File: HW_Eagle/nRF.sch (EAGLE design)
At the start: 24 parts, among them X1 B4B-ZR

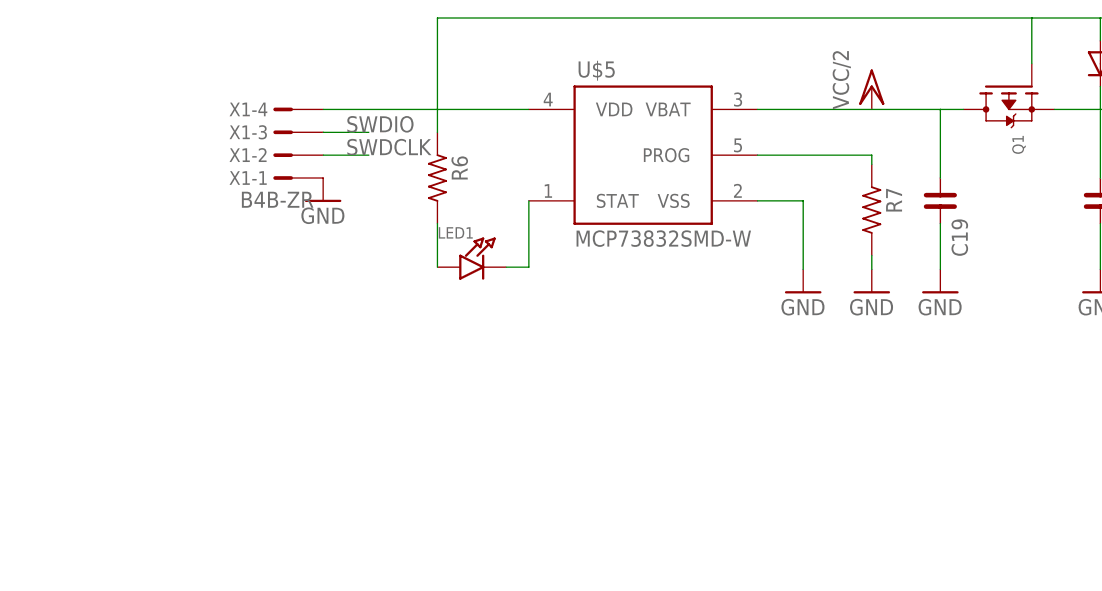
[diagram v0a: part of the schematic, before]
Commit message: [HW] Add Batterry connector
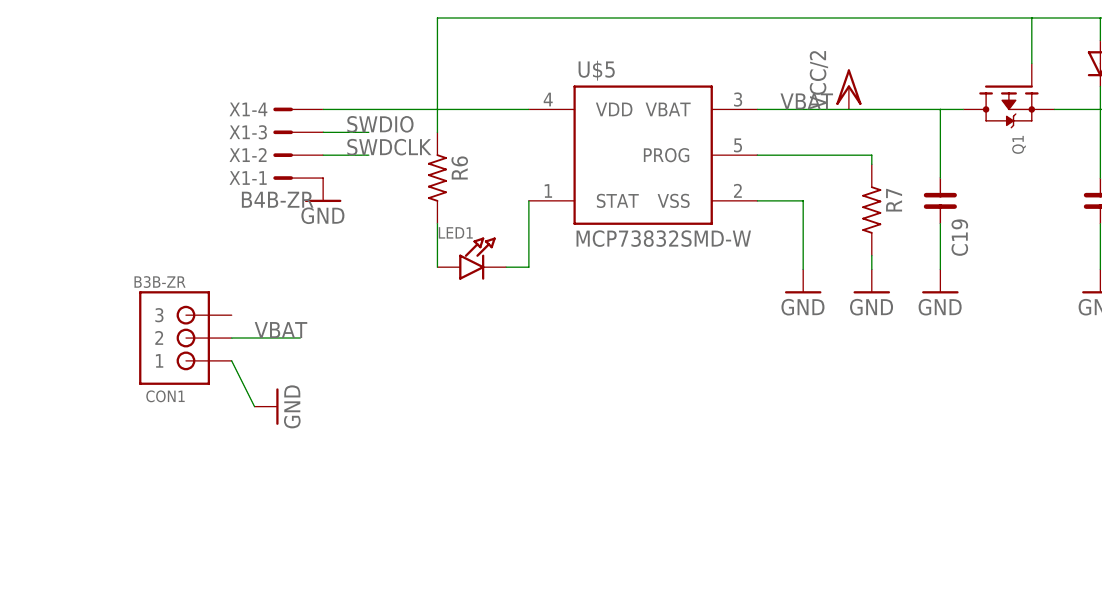
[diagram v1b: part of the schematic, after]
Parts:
- added CON1: B3B-ZR, jst:B3B-ZR
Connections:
- net GND: now also CON1.1
- net VBAT: now also CON1.2
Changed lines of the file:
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@@
 <grid distance="0.1" unitdist="inch" unit="inch" style="lines" multiple="1" display="no" altdistance="0.01" altunitdist="inch" altunit="inch"/>
 <layers>
-<layer number="1" name="Top" color="4" fill="1" visible="yes" active="no"/>
-<layer number="16" name="Bottom" color="1" fill="1" visible="yes" active="no"/>
-<layer number="17" name="Pads" color="2" fill="1" visible="yes" active="no"/>
-<layer number="18" name="Vias" color="2" fill="1" visible="yes" active="no"/>
-<layer number="19" name="Unrouted" color="6" fill="1" visible="yes" active="no"/>
-<layer number="20" name="Dimension" color="15" fill="1" visible="yes" active="no"/>
-<layer number="21" name="tPlace" color="7" fill="1" visible="yes" active="no"/>
-<layer number="22" name="bPlace" color="7" fill="1" visible="yes" active="no"/>
-<layer number="23" name="tOrigins" color="15" fill="1" visible="yes" active="no"/>
-<layer number="24" name="bOrigins" color="15" fill="1" visible="yes" active="no"/>
-<layer number="25" name="tNames" color="7" fill="1" visible="yes" active="no"/>
-<layer number="26" name="bNames" color="7" fill="1" visible="yes" active="no"/>
-<layer number="27" name="tValues" color="7" fill="1" visible="yes" active="no"/>
-<layer number="28" name="bValues" color="7" fill="1" visible="yes" active="no"/>
+<layer number="1" name="Top" color="4" fill="1" visible="no" active="no"/>
+<layer number="16" name="Bottom" color="1" fill="1" visible="no" active="no"/>
+<layer number="17" name="Pads" color="2" fill="1" visible="no" active="no"/>
+<layer number="18" name="Vias" color="2" fill="1" visible="no" active="no"/>
+<layer number="19" name="Unrouted" color="6" fill="1" visible="no" active="no"/>
+<layer number="20" name="Dimension" color="15" fill="1" visible="no" active="no"/>
+<layer number="21" name="tPlace" color="7" fill="1" visible="no" active="no"/>
+<layer number="22" name="bPlace" color="7" fill="1" visible="no" active="no"/>
+<layer number="23" name="tOrigins" color="15" fill="1" visible="no" active="no"/>
+<layer number="24" name="bOrigins" color="15" fill="1" visible="no" active="no"/>
+<layer number="25" name="tNames" color="7" fill="1" visible="no" active="no"/>
+<layer number="26" name="bNames" color="7" fill="1" visible="no" active="no"/>
+<layer number="27" name="tValues" color="7" fill="1" visible="no" active="no"/>
+<layer number="28" name="bValues" color="7" fill="1" visible="no" active="no"/>
 <layer number="29" name="tStop" color="7" fill="3" visible="no" active="no"/>
 <layer number="30" name="bStop" color="7" fill="6" visible="no" active="no"/>
@@
 <layer number="35" name="tGlue" color="7" fill="4" visible="no" active="no"/>
 <layer number="36" name="bGlue" color="7" fill="5" visible="no" active="no"/>
-<layer number="37" name="tTest" color="7" fill="1" visible="yes" active="no"/>
-<layer number="38" name="bTest" color="7" fill="1" visible="yes" active="no"/>
+<layer number="37" name="tTest" color="7" fill="1" visible="no" active="no"/>
+<layer number="38" name="bTest" color="7" fill="1" visible="no" active="no"/>
 <layer number="39" name="tKeepout" color="4" fill="11" visible="no" active="no"/>
 <layer number="40" name="bKeepout" color="1" fill="11" visible="no" active="no"/>
@@
 <layer number="44" name="Drills" color="7" fill="1" visible="no" active="no"/>
 <layer number="45" name="Holes" color="7" fill="1" visible="no" active="no"/>
-<layer number="46" name="Milling" color="3" fill="1" visible="yes" active="no"/>
-<layer number="47" name="Measures" color="7" fill="1" visible="yes" active="no"/>
-<layer number="48" name="Document" color="7" fill="1" visible="yes" active="no"/>
-<layer number="49" name="Reference" color="7" fill="1" visible="yes" active="no"/>
-<layer number="50" name="dxf" color="7" fill="1" visible="yes" active="no"/>
-<layer number="51" name="tDocu" color="7" fill="1" visible="yes" active="no"/>
-<layer number="52" name="bDocu" color="7" fill="1" visible="yes" active="no"/>
-<layer number="53" name="tGND_GNDA" color="7" fill="9" visible="yes" active="no"/>
-<layer number="54" name="bGND_GNDA" color="1" fill="9" visible="yes" active="no"/>
-<layer number="56" name="wert" color="7" fill="1" visible="yes" active="no"/>
+<layer number="46" name="Milling" color="3" fill="1" visible="no" active="no"/>
+<layer number="47" name="Measures" color="7" fill="1" visible="no" active="no"/>
+<layer number="48" name="Document" color="7" fill="1" visible="no" active="no"/>
+<layer number="49" name="Reference" color="7" fill="1" visible="no" active="no"/>
+<layer number="50" name="dxf" color="7" fill="1" visible="no" active="no"/>
+<layer number="51" name="tDocu" color="7" fill="1" visible="no" active="no"/>
+<layer number="52" name="bDocu" color="7" fill="1" visible="no" active="no"/>
+<layer number="53" name="tGND_GNDA" color="7" fill="9" visible="no" active="no"/>
+<layer number="54" name="bGND_GNDA" color="1" fill="9" visible="no" active="no"/>
+<layer number="56" name="wert" color="7" fill="1" visible="no" active="no"/>
 <layer number="90" name="Modules" color="5" fill="1" visible="yes" active="yes"/>
 <layer number="91" name="Nets" color="2" fill="1" visible="yes" active="yes"/>
@@
 <part name="GND1" library="supply1" deviceset="GND" device=""/>
 <part name="GND2" library="supply1" deviceset="GND" device=""/>
+<part name="GND3" library="supply1" deviceset="GND" device=""/>
+<part name="CON1" library="jst" deviceset="B3B-ZR" device=""/>
 </parts>
 <sheets>
@@
 <instance part="GND25" gate="1" x="-83.82" y="165.1"/>
 <instance part="GND26" gate="1" x="-30.48" y="154.94"/>
-<instance part="P+9" gate="G$1" x="-22.86" y="177.8"/>
+<instance part="P+9" gate="G$1" x="-25.4" y="177.8"/>
 <instance part="R6" gate="G$1" x="-71.12" y="167.64" rot="R270"/>
 <instance part="C19" gate="G$1" x="-15.24" y="165.1" rot="R270"/>
@@
 <instance part="GND1" gate="1" x="-17.78" y="93.98" rot="R270"/>
 <instance part="GND2" gate="1" x="-17.78" y="68.58" rot="R270"/>
+<instance part="GND3" gate="1" x="-88.9" y="142.24" rot="R90"/>
+<instance part="CON1" gate="G$1" x="-101.6" y="149.86" rot="R180"/>
 </instances>
 <busses>
@@
 <pinref part="GND2" gate="1" pin="GND"/>
 </segment>
+<segment>
+<pinref part="CON1" gate="G$1" pin="1"/>
+<pinref part="GND3" gate="1" pin="GND"/>
+<wire x1="-91.44" y1="142.24" x2="-93.98" y2="147.32" width="0.1524" layer="91"/>
+</segment>
 </net>
 <net name="VCC" class="0">
@@
 <segment>
 <pinref part="U$5" gate="G$1" pin="VBAT"/>
-<wire x1="-22.86" y1="175.26" x2="-35.56" y2="175.26" width="0.1524" layer="91"/>
+<wire x1="-25.4" y1="175.26" x2="-35.56" y2="175.26" width="0.1524" layer="91"/>
 <pinref part="P+9" gate="G$1" pin="VCC/2"/>
 <pinref part="C19" gate="G$1" pin="1"/>
-<wire x1="-22.86" y1="175.26" x2="-15.24" y2="175.26" width="0.1524" layer="91"/>
+<wire x1="-25.4" y1="175.26" x2="-15.24" y2="175.26" width="0.1524" layer="91"/>
 <wire x1="-15.24" y1="175.26" x2="-15.24" y2="167.64" width="0.1524" layer="91"/>
 <pinref part="Q1" gate="G$1" pin="D"/>
 <wire x1="-12.7" y1="175.26" x2="-15.24" y2="175.26" width="0.1524" layer="91"/>
-</segment>
-</net>
+<label x="-33.02" y="175.26" size="1.778" layer="95"/>
+</segment>
+<segment>
+<pinref part="CON1" gate="G$1" pin="2"/>
+<wire x1="-86.36" y1="149.86" x2="-93.98" y2="149.86" width="0.1524" layer="91"/>
+<label x="-91.44" y="149.86" size="1.778" layer="95"/>
+</segment>
+</net>

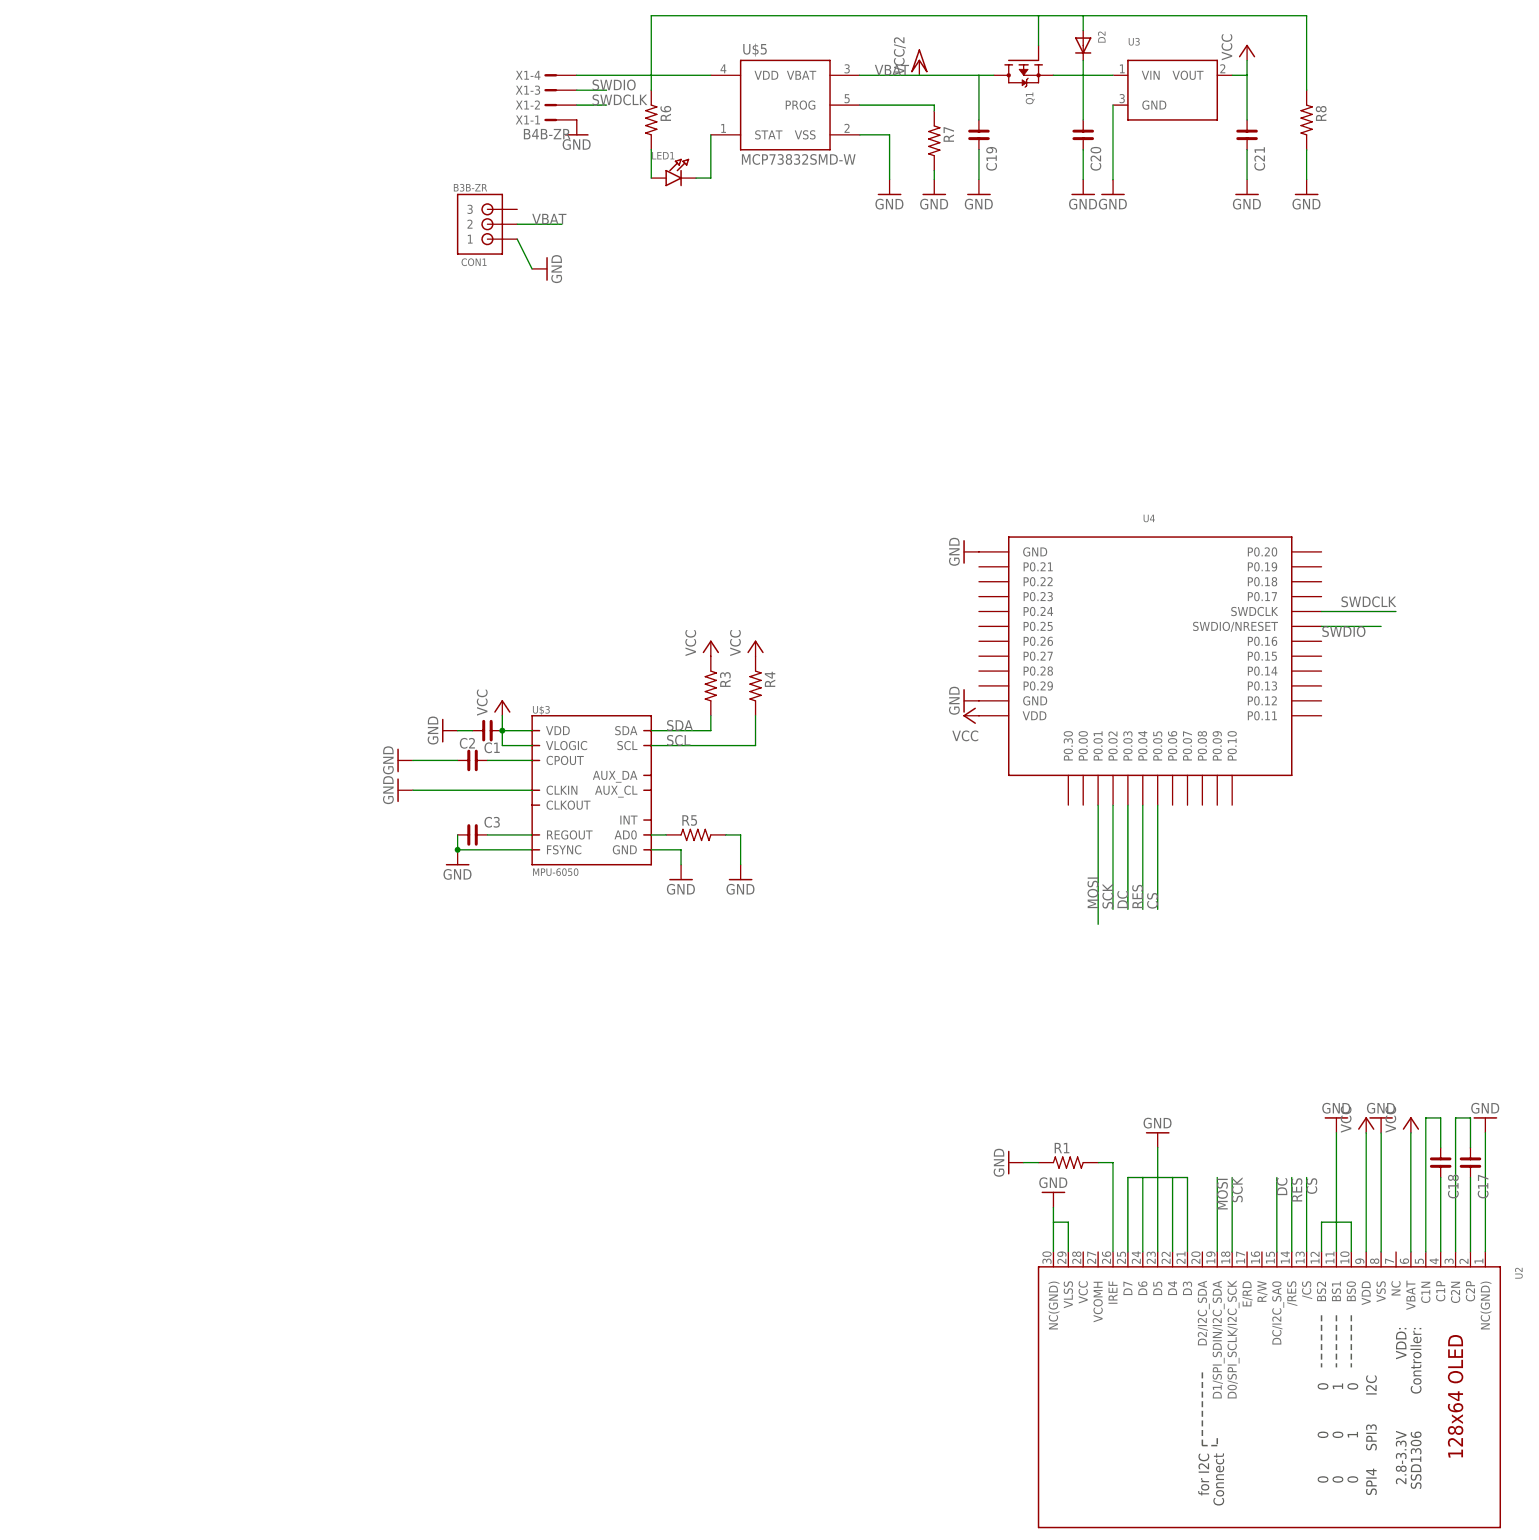
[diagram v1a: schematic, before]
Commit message: [HW] Change to using modules
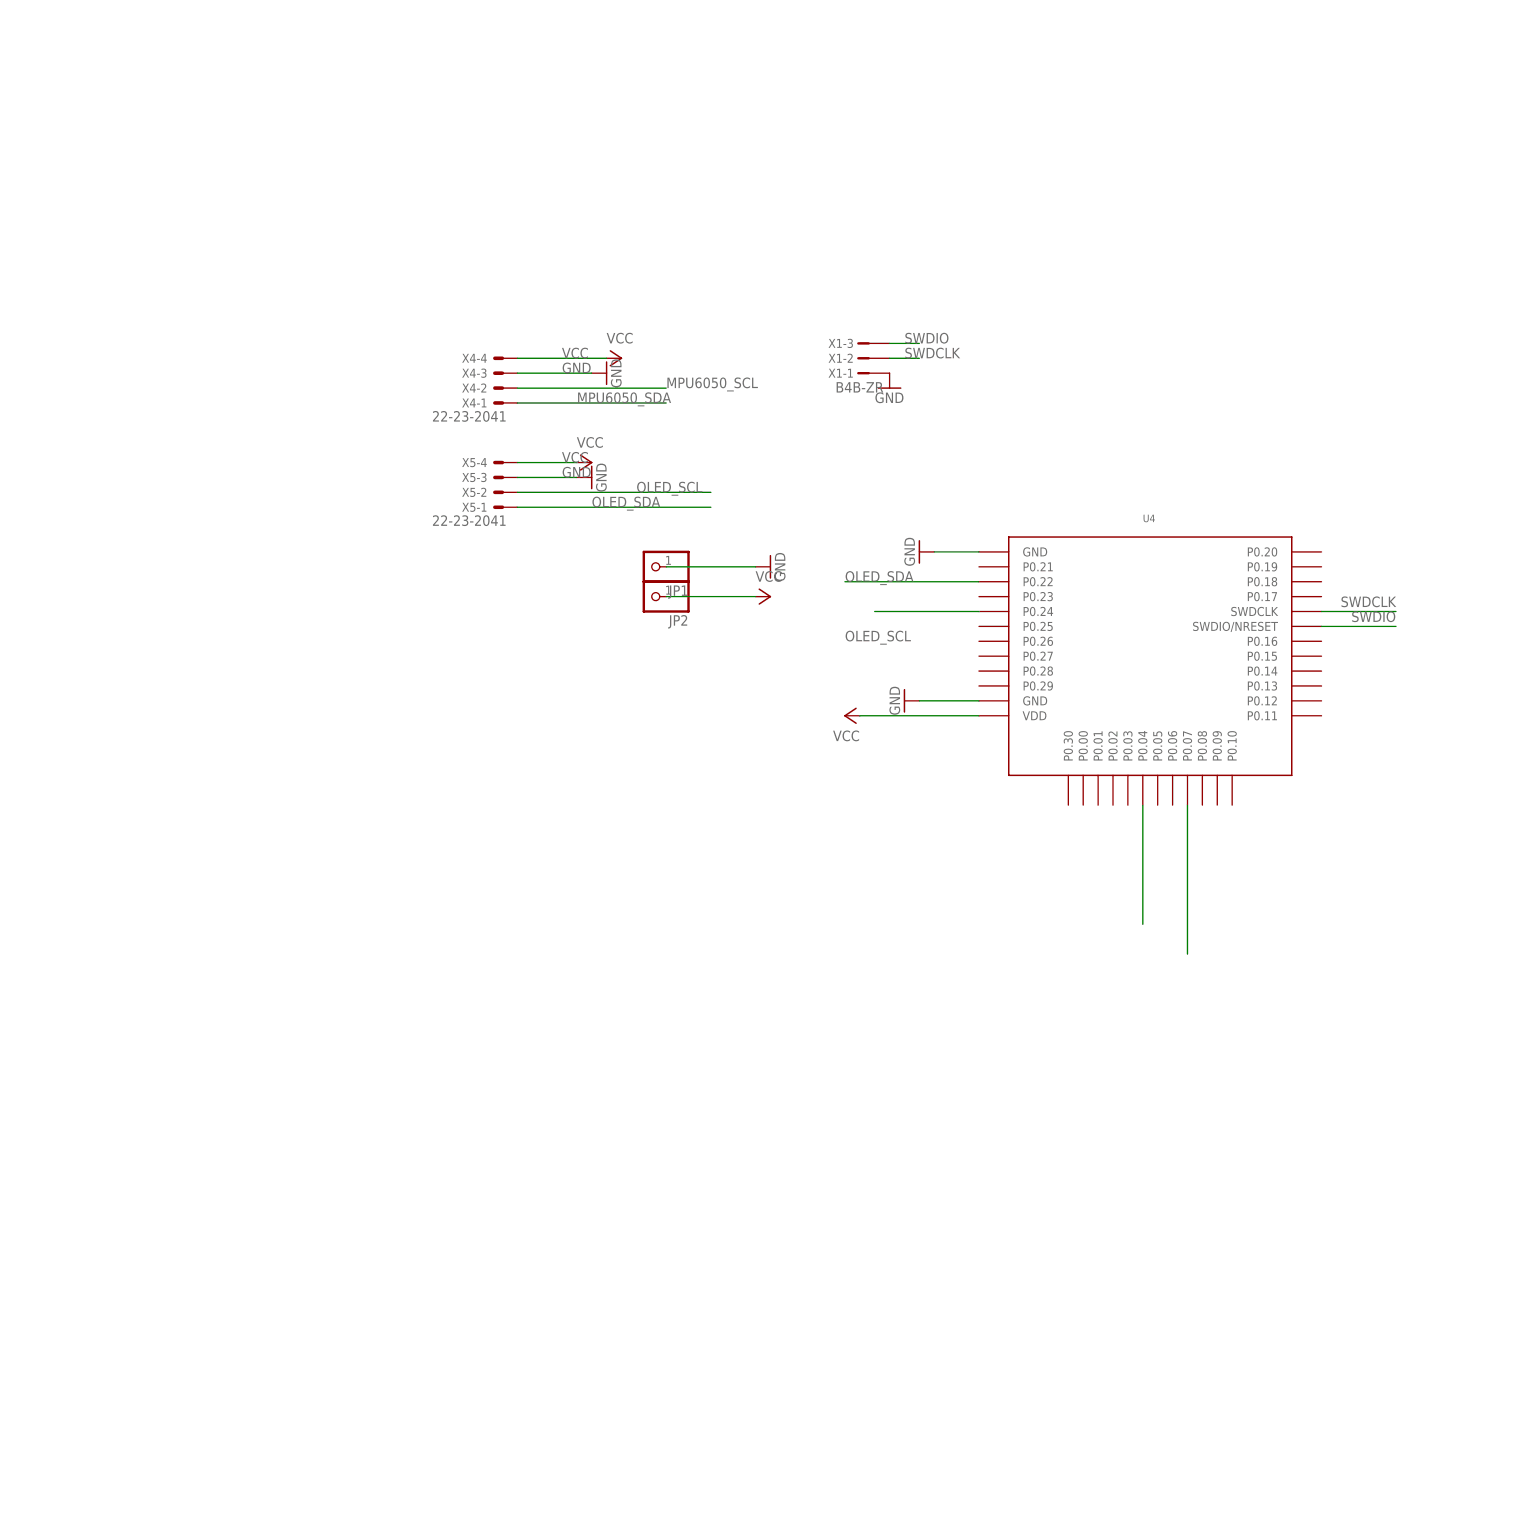
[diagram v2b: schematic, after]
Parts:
- removed C1, C17, C18, C19, C2, C20, C21, C3: (no value), rc-master-smd:C_0402
- removed CON1: B3B-ZR, jst:B3B-ZR
- removed D2: (no value), microbuilder:DIODESOD-123
- removed LED1: (no value), microbuilder:LED0603
- removed Q1: (no value), microbuilder:MOSFET-P
- removed R1, R3, R4, R5, R6, R7, R8: (no value), rc-master-smd:R_0402
- removed U$3: MPU-6050, invensense:MPU-6050
- removed U$5: MCP73832SMD-W, NicShackle:MCP73832SMD-W
- removed U2: (no value), microbuilder:DISP_OLED_UG-2864HSWEG010.96"
- removed U3: (no value), microbuilder:VREG_SOT23SOT23_WIDE
- added JP1, JP2: (no value), pinhead:PINHD-1X1
- added X4, X5: 22-23-2041, con-molex:22-23-2041
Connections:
- removed net CS: U2./CS, U4.P0.05
- removed net DC: U2.DC/I2C_SA0, U4.P0.03
- removed net MOSI: U2.D1/SPI_SDIN/I2C_SDA, U4.P0.01
- removed net N$13: R5.1, U$3.AD0
- removed net N$14: C3.2, U$3.REGOUT
- removed net N$15: D2.A, Q1.G, R6.1, R8.1, U$5.VDD, X1-4.1
- removed net N$16: LED1.C, U$5.STAT
- removed net N$17: C17.2, U2.C2P
- removed net N$18: C1.2, U$3.CPOUT
- removed net N$19: C18.2, U2.C1P
- removed net N$20: C17.1, U2.C2N
- removed net N$21: C18.1, U2.C1N
- removed net N$22: R1.2, U2.IREF
- removed net N$23: LED1.A, R6.2
- removed net N$24: R7.1, U$5.PROG
- removed net N$25: C20.1, D2.C, Q1.S, U3.VIN
- removed net RES: U2./RES, U4.P0.04
- removed net SCK: U2.D0/SPI_SCLK/I2C_SCK, U4.P0.02
- removed net SCL: R4.2, U$3.SCL
- removed net SDA: R3.2, U$3.SDA
- removed net VBAT: C19.1, CON1.2, Q1.D, U$5.VBAT
- new net MPU6050_SCL: U4.P0.04, X4-2.S
- new net MPU6050_SDA: U4.P0.07, X4-1.S
- new net OLED_SCL: U4.P0.24, X5-2.S
- new net OLED_SDA: U4.P0.22, X5-1.S
- net GND: now also JP1.1, X4-3.S, X5-3.S; no longer C1.1, C19.2, C2.2, C20.2, C21.2, C3.1, CON1.1, R1.1, R5.2, R7.2, R8.2, U$3.CLKIN, U$3.FSYNC, U$3.GND, U$5.VSS, U2.BS0, U2.BS1, U2.BS2, U2.D3, U2.D4, U2.D5, U2.D6, U2.D7, U2.NC(GND)@1, U2.NC(GND)@2, U2.VLSS, U2.VSS, U3.GND
- net VCC: now also JP2.1, X4-4.S, X5-4.S; no longer C2.1, C21.1, R3.1, R4.1, U$3.VDD, U$3.VLOGIC, U2.VBAT, U2.VDD, U3.VOUT
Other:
- moved on the sheet: X1-1, X1-2, X1-3
